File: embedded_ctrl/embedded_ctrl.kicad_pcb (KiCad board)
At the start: 2 copper layers, 67.8 x 54.5 mm, 15 parts, among them J1 Conn_02x13_Odd_Even, J3 Conn_01x15_Socket, J4 Conn_01x15_Socket, J6 Screw_Terminal_01x02

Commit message: more work on embedded ctrlr
same-o
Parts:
- removed J3, J4: Conn_01x15_Socket, Connector_PinSocket_2.54mm:PinSocket_1x15_P2.54mm_Vertical
- added C6: 100nF, Capacitor_SMD:C_0603_1608Metric, F.Cu at (134.1, 86.1)
- added C7: 100nF, Capacitor_SMD:C_0603_1608Metric, F.Cu at (131.1, 87.6)
- added C8: 100nF, Capacitor_SMD:C_0603_1608Metric, F.Cu at (101.6, 80.3)
- added C9: 10uF, Capacitor_SMD:CP_Elec_5x5.8, F.Cu at (136.9, 57.8)
- added D1: D_TVS, Diode_SMD:D_0603_1608Metric, F.Cu at (100.1, 80.3)
- added D2: D_TVS, Diode_SMD:D_0603_1608Metric, F.Cu at (100.1, 74.9)
- added D3: D_TVS, Diode_SMD:D_0603_1608Metric, F.Cu at (100.1, 83.6)
- added D4: LED, Diode_SMD:D_0603_1608Metric, F.Cu at (137.7, 52.0)
- added J7: USB_B, Connector_USB:USB_B_OST_USB-B1HSxx_Horizontal, F.Cu at (96.7, 81.7)
- added Q1: SS8050, Package_TO_SOT_SMD:SOT-23, F.Cu at (104.1, 65.0)
- added Q2: SS8050, Package_TO_SOT_SMD:SOT-23, F.Cu at (109.2, 68.6)
- added R10: 0R, Resistor_SMD:R_0603_1608Metric, F.Cu at (105.7, 72.4)
- added R11: 0R, Resistor_SMD:R_0603_1608Metric, F.Cu at (105.7, 70.9)
- added R12: 10k, Resistor_SMD:R_0603_1608Metric, F.Cu at (103.4, 68.5)
- added R13: 10k, Resistor_SMD:R_0603_1608Metric, F.Cu at (105.7, 67.8)
- added R14: 0R, Resistor_SMD:R_0603_1608Metric, F.Cu at (105.7, 69.3)
- added R15: 2k (5%), Resistor_SMD:R_0603_1608Metric, F.Cu at (135.9, 52.1)
- added R5: 10k, Resistor_SMD:R_0603_1608Metric, F.Cu at (132.6, 86.1)
- added R6: 22.1k (1%), Resistor_SMD:R_0603_1608Metric, F.Cu at (102.9, 82.8)
- added R7: 47.5k (1%), Resistor_SMD:R_0603_1608Metric, F.Cu at (102.9, 84.3)
- added R8: 2k (5%), Resistor_SMD:R_0603_1608Metric, F.Cu at (104.1, 81.0)
- added R9: DNP, Resistor_SMD:R_0603_1608Metric, F.Cu at (106.9, 81.9)
- added REF**: RJ14_Connfly_DS1133-S4_Horizontal, Connector_RJ:RJ14_Connfly_DS1133-S4_Horizontal, F.Cu at (93.7, 39.9)
- added U1: ESP32-WROOM-32, RF_Module:ESP32-WROOM-32, F.Cu at (120.0, 79.9)
- added U2: CP2102N-A02-GQFN28, Package_DFN_QFN:QFN-28-1EP_5x5mm_P0.5mm_EP3.35x3.35mm, F.Cu at (105.2, 76.6)
- added U3: R-78E3.3-1.0, Converter_DCDC:Converter_DCDC_RECOM_R-78E-0.5_THT, F.Cu at (110.7, 59.1)
- moved C5 42.1 mm to (100.6, 54.6), turned to -90 degrees
- moved J6 32.2 mm to (130.8, 55.1)
- moved C2 29.5 mm to (139.4, 84.1), turned to 0 degrees
- moved C3 29.1 mm to (139.4, 86.9), turned to 0 degrees
- moved R2 28.2 mm to (136.4, 84.1), turned to 0 degrees
- moved C4 27.0 mm to (138.1, 88.4), turned to 0 degrees
- moved R3 25.9 mm to (136.4, 86.9), turned to 0 degrees
- moved C1 24.4 mm to (139.4, 82.3), turned to 0 degrees
- moved R4 24.4 mm to (135.1, 88.4), turned to 0 degrees
- moved R1 22.9 mm to (136.4, 82.3), turned to 0 degrees
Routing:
- net 5V: track 0.00 -> 32.2 mm
- net 3V3: track 0.00 -> 30.2 mm, vias 0 -> 1
- net /RXD0_ESP: track 0.00 -> 15.3 mm
- net /TXD0_ESP: track 0.00 -> 14.9 mm
- net /~{RTS}: track 0.00 -> 8.76 mm
- net D34: track 0.00 -> 8.64 mm
- net D35: track 0.00 -> 7.94 mm
- net D19: track 0.00 -> 7.76 mm
- net D32: track 0.00 -> 7.17 mm
- net /~{DTR}: track 0.00 -> 6.48 mm
- net Net-(U2-VBUS): track 0.00 -> 5.61 mm
- net EN: track 0.00 -> 5.49 mm
- net /TXD_BRIDGE: track 0.00 -> 4.35 mm
- net /IO0: track 0.00 -> 3.48 mm
- net Net-(U2-~{SUSPEND}): track 0.00 -> 2.98 mm
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
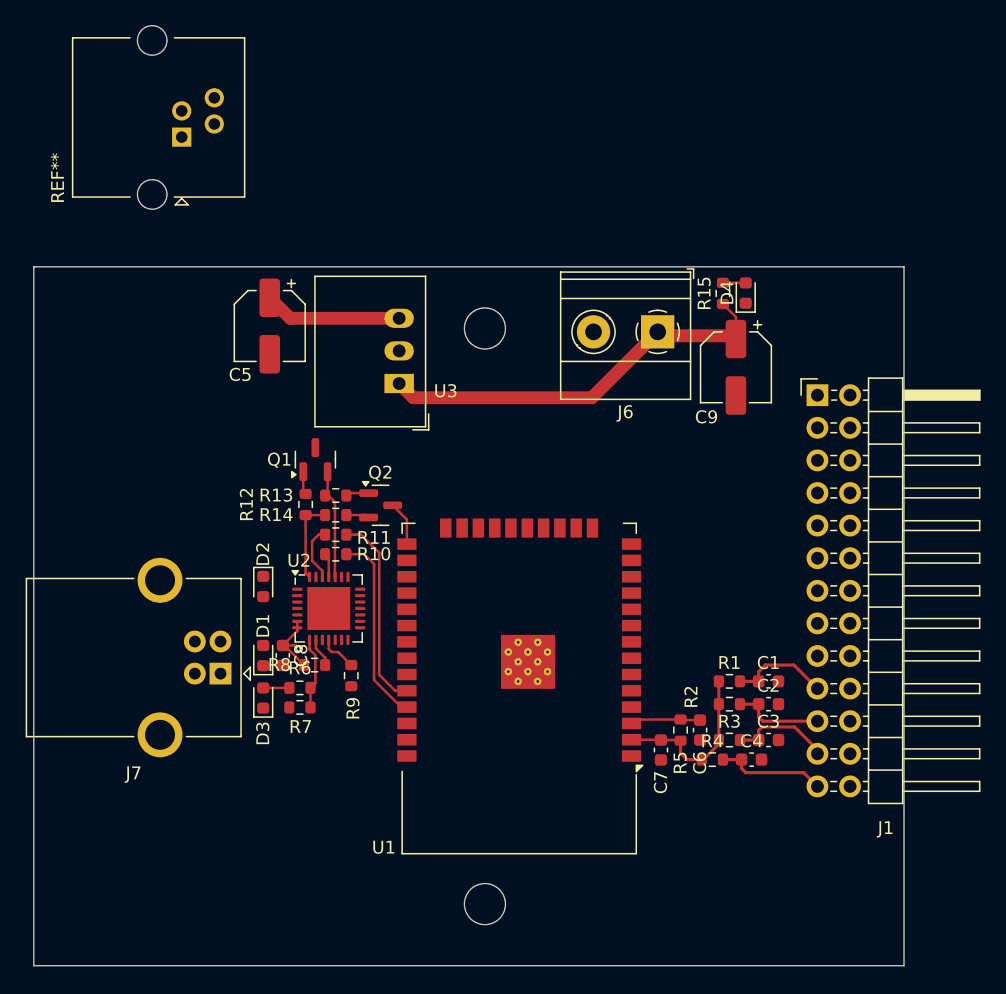
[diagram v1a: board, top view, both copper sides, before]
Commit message: add rj11 connectors for pendants
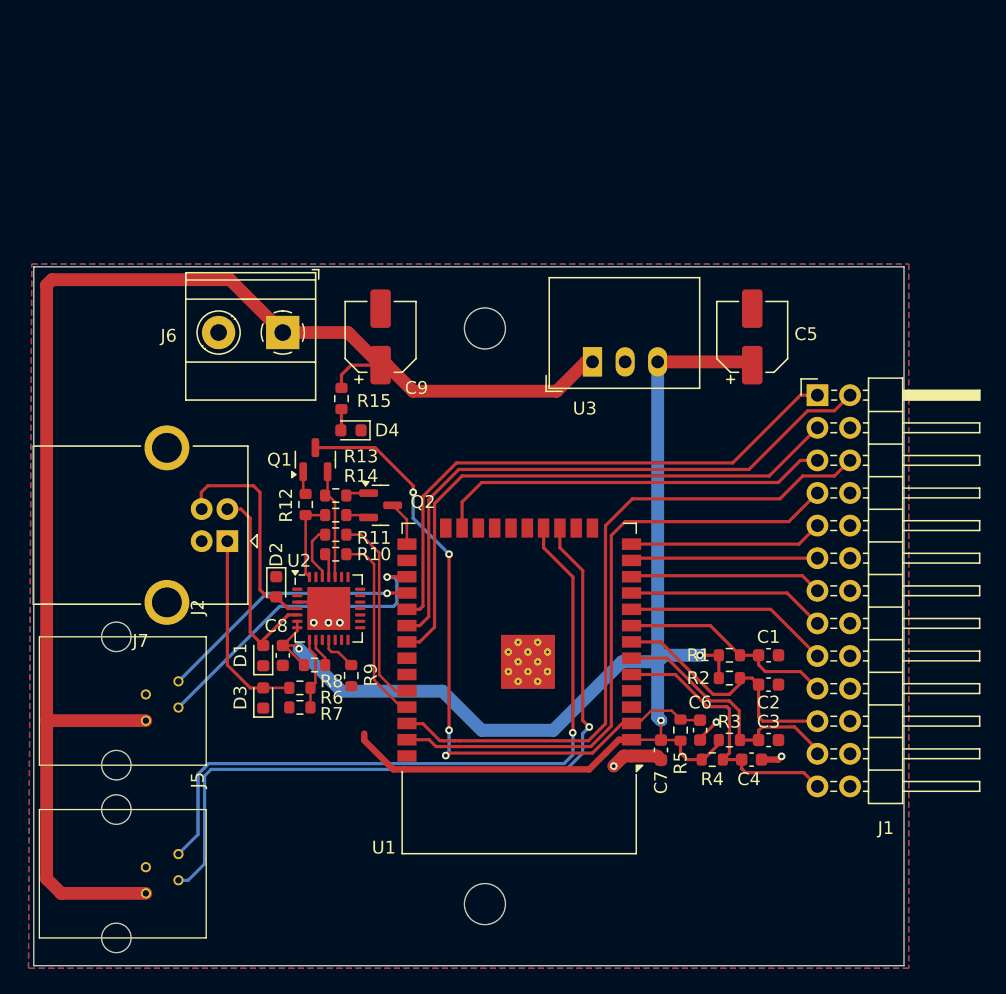
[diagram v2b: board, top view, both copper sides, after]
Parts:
- removed REF**: RJ14_Connfly_DS1133-S4_Horizontal, Connector_RJ:RJ14_Connfly_DS1133-S4_Horizontal
- added J2: RJ11, Library:RJ11_C189737, F.Cu at (93.5, 83.8)
- added J5: RJ11, Library:RJ11_C189737, F.Cu at (93.5, 97.3)
- C5, C9: footprint Capacitor_SMD:CP_Elec_5x5.8 -> Capacitor_SMD:CP_Elec_5x5.4
- moved C5 37.6 mm to (138.2, 55.5), turned to 90 degrees
- moved D4 32.6 mm to (106.9, 62.7), turned to 180 degrees
- moved R15 30.8 mm to (106.2, 60.3), turned to -90 degrees
- moved J6 29.2 mm to (101.6, 55.1)
- moved C9 27.8 mm to (109.2, 55.5), turned to 90 degrees
- moved U3 15.2 mm to (125.7, 57.4), turned to 0 degrees
- moved J7 10.3 mm to (97.3, 71.4)
- moved C1 2.03 mm to (139.4, 80.3)
- moved R1 2.03 mm to (136.4, 80.3)
- moved R2 2.03 mm to (136.4, 82.0)
- moved C2 1.52 mm to (139.4, 82.5)
- moved D2 1.02 mm to (101.1, 74.9)
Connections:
- C1 pad 1: D19 -> D33
- J1 pad 11: D26 -> D14
- J1 pad 15: D33 -> D26
- J1 pad 19: D19 -> D33
- J1 pad 3: D22 -> D19
- J1 pad 6: D23 -> D22
- J1 pad 7: D14 -> D23
- R1 pad 2: D19 -> D33
- U1 pad 10: unconnected-(U1-IO25-Pad10) -> D25
- U1 pad 11: unconnected-(U1-IO26-Pad11) -> D26
- U1 pad 12: unconnected-(U1-IO27-Pad12) -> D27
- U1 pad 13: unconnected-(U1-IO14-Pad13) -> D14
- U1 pad 14: unconnected-(U1-IO12-Pad14) -> D12
- U1 pad 17: unconnected-(U1-SHD/SD2-Pad17) -> /U1RXD
- U1 pad 18: unconnected-(U1-SWP/SD3-Pad18) -> /U1TXD
- U1 pad 23: unconnected-(U1-IO15-Pad23) -> D15
- U1 pad 27: unconnected-(U1-IO16-Pad27) -> /U2RXD
- U1 pad 28: unconnected-(U1-IO17-Pad28) -> /U2TXD
- U1 pad 29: unconnected-(U1-IO5-Pad29) -> D5
- U1 pad 30: unconnected-(U1-IO18-Pad30) -> D18
- U1 pad 31: unconnected-(U1-IO19-Pad31) -> D19
- U1 pad 36: unconnected-(U1-IO22-Pad36) -> D22
- U1 pad 37: unconnected-(U1-IO23-Pad37) -> D23
- U1 pad 6: unconnected-(U1-IO34-Pad6) -> D34
- U1 pad 7: unconnected-(U1-IO35-Pad7) -> D35
- U1 pad 8: unconnected-(U1-IO32-Pad8) -> D32
- U1 pad 9: unconnected-(U1-IO33-Pad9) -> D33
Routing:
- net 3V3: track 30.2 -> 115.2 mm, vias 1 -> 3
- net 5V: track 32.2 -> 113.8 mm
- net /U1RXD: track 0.00 -> 58.3 mm, vias 0 -> 1
- net /U1TXD: track 0.00 -> 55.3 mm, vias 0 -> 1
- net D22: track 0.00 -> 53.2 mm
- net D23: track 0.00 -> 49.1 mm
- net D18: track 0.00 -> 47.3 mm
- net EN: track 5.49 -> 52.7 mm, vias 0 -> 4
- net D5: track 0.00 -> 43.9 mm
- net D19: track 7.76 -> 44.5 mm
- net D15: track 0.00 -> 31.1 mm
- net /U2RXD: track 0.00 -> 24.6 mm, vias 0 -> 1
- net /U2TXD: track 0.00 -> 20.6 mm, vias 0 -> 1
- net /D+: track 0.00 -> 17.4 mm
- net D33: track 0.00 -> 17.0 mm
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- added copper zone on B.Cu, net GND
- added copper zone on F.Cu, net GND

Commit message: improve pcb layout
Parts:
- moved R1 3.31 mm to (139.7, 80.5), turned to 90 degrees
- moved C1 3.16 mm to (136.6, 78.9), turned to -90 degrees
- moved R7 3.10 mm to (105.9, 85.2), turned to 90 degrees
- moved R6 2.77 mm to (104.4, 85.2), turned to 90 degrees
- moved D3 2.75 mm to (100.3, 86.3), turned to -90 degrees
- moved R2 2.70 mm to (139.0, 82.9), turned to 180 degrees
- moved C2 2.44 mm to (138.2, 80.5), turned to 90 degrees
- moved R8 1.44 mm to (105.1, 82.0)
- moved C6 1.27 mm to (134.1, 84.8)
- moved R5 1.27 mm to (132.6, 84.8)
- moved C3 1.27 mm to (139.4, 85.6)
- moved C4 1.27 mm to (138.1, 87.1)
- moved C7 1.27 mm to (131.1, 86.4)
- moved R3 1.27 mm to (136.4, 85.6)
- moved R4 1.27 mm to (135.1, 87.1)
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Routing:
- net 3V3: track 115.2 -> 135.7 mm, vias 3 -> 0
- net /VBUS: track 15.2 -> 24.4 mm, vias 0 -> 2
- net Net-(U2-VBUS): track 5.61 -> 7.71 mm
- net Net-(U2-~{RST}): track 2.26 -> 3.69 mm
- net D32: track 19.8 -> 18.8 mm
- net EN: track 52.7 -> 53.5 mm
- net Net-(U2-~{SUSPEND}): track 2.98 -> 3.51 mm
- net GND: track 10.4 -> 10.7 mm, vias 6 -> 34

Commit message: same
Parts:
- added TP1: VBUS, TestPoint:TestPoint_THTPad_D1.0mm_Drill0.5mm, F.Cu at (99.9, 86.2)
- added TP2: 3V3, TestPoint:TestPoint_THTPad_D1.0mm_Drill0.5mm, F.Cu at (140.7, 94.6)
- added TP3: 5V, TestPoint:TestPoint_THTPad_D1.0mm_Drill0.5mm, F.Cu at (134.4, 64.1)
- added TP4: GND, TestPoint:TestPoint_THTPad_D1.0mm_Drill0.5mm, F.Cu at (111.5, 55.0)
- moved C5 43.1 mm to (144.7, 98.0), turned to -90 degrees
- moved J6 27.3 mm to (128.9, 55.0)
- moved C9 19.3 mm to (126.6, 63.8), turned to 180 degrees
- moved R15 13.9 mm to (120.0, 61.7), turned to 180 degrees
- moved U3 13.3 mm to (138.9, 59.5), turned to 90 degrees
- moved D4 9.58 mm to (116.4, 61.7), turned to 0 degrees
- moved D3 4.22 mm to (97.7, 83.1), turned to 180 degrees
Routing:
- net 5V: track 113.8 -> 145.4 mm
- net 3V3: track 135.7 -> 133.4 mm
- net /VBUS: track 24.4 -> 25.2 mm, vias 2 -> 1
- net GND: vias 34 -> 63

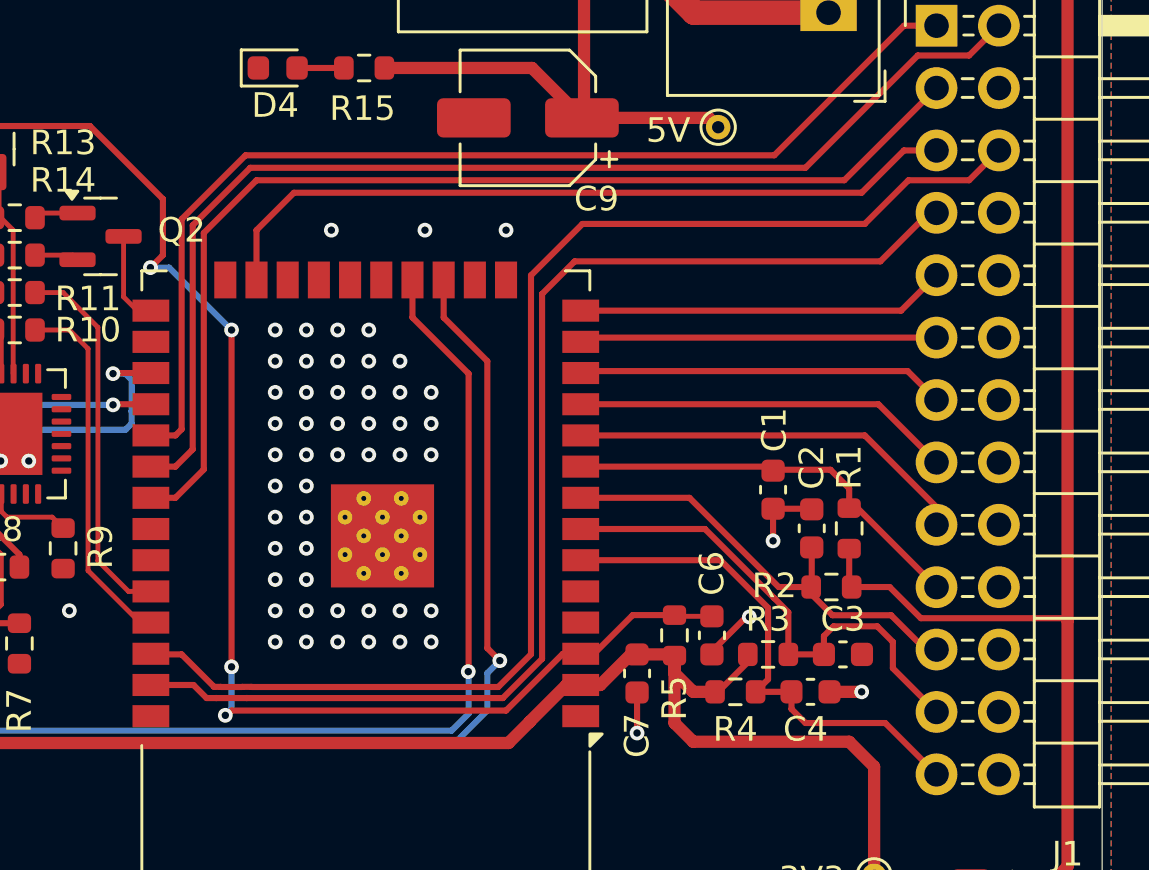
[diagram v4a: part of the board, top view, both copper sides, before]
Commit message: Reassign pins to free up JTAG pins, just in case
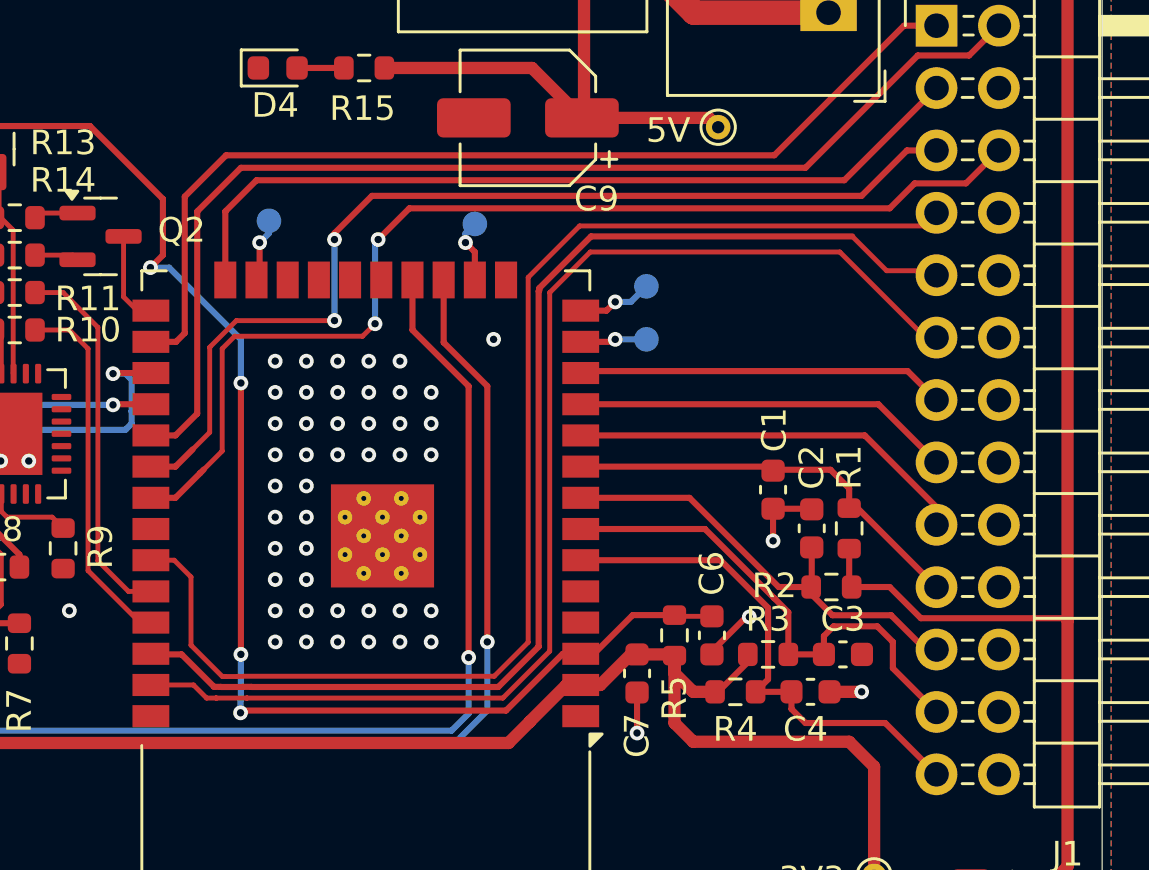
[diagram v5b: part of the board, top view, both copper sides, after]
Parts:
- added TP5: MTDI, TestPoint:TestPoint_Pad_D1.0mm, B.Cu at (131.4, 70.6)
- added TP6: MTCK, TestPoint:TestPoint_Pad_D1.0mm, B.Cu at (124.5, 68.1)
- added TP7: MTMS, TestPoint:TestPoint_Pad_D1.0mm, B.Cu at (131.4, 72.8)
- added TP8: MTDO, TestPoint:TestPoint_Pad_D1.0mm, B.Cu at (116.1, 67.9)
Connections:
- J1 pad 1: D5 -> D4
- J1 pad 11: D14 -> D23
- J1 pad 2: D18 -> D5
- J1 pad 3: D19 -> D2
- J1 pad 5: D15 -> D18
- J1 pad 6: D22 -> D19
- J1 pad 7: D23 -> D21
- J1 pad 9: D12 -> D22
- U1 pad 13: D14 -> /MTMS
- U1 pad 14: D12 -> /MTDI
- U1 pad 16: unconnected-(U1-IO13-Pad16) -> /MTCK
- U1 pad 23: D15 -> /MTDO
- U1 pad 24: unconnected-(U1-IO2-Pad24) -> D2
- U1 pad 26: unconnected-(U1-IO4-Pad26) -> D4
- U1 pad 33: unconnected-(U1-IO21-Pad33) -> D21
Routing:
- net D21: track 0.00 -> 52.1 mm
- net D4: track 0.00 -> 40.6 mm
- net D2: track 0.00 -> 33.8 mm
- net D15: track 31.1 -> 0.00 mm
- net D12: track 15.1 -> 0.00 mm
- net D14: track 14.6 -> 0.00 mm
- net D18: track 47.3 -> 41.4 mm, vias 0 -> 2
- net D22: track 53.2 -> 49.3 mm
- net /MTDI: track 0.00 -> 3.09 mm, vias 0 -> 1
- net /MTMS: track 0.00 -> 2.72 mm, vias 0 -> 1
- net /MTDO: track 0.00 -> 2.62 mm, vias 0 -> 1
- net /MTCK: track 0.00 -> 2.60 mm, vias 0 -> 1
- net D5: track 43.9 -> 46.3 mm
- net EN: track 53.5 -> 52.8 mm
- net D23: track 49.1 -> 49.7 mm
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
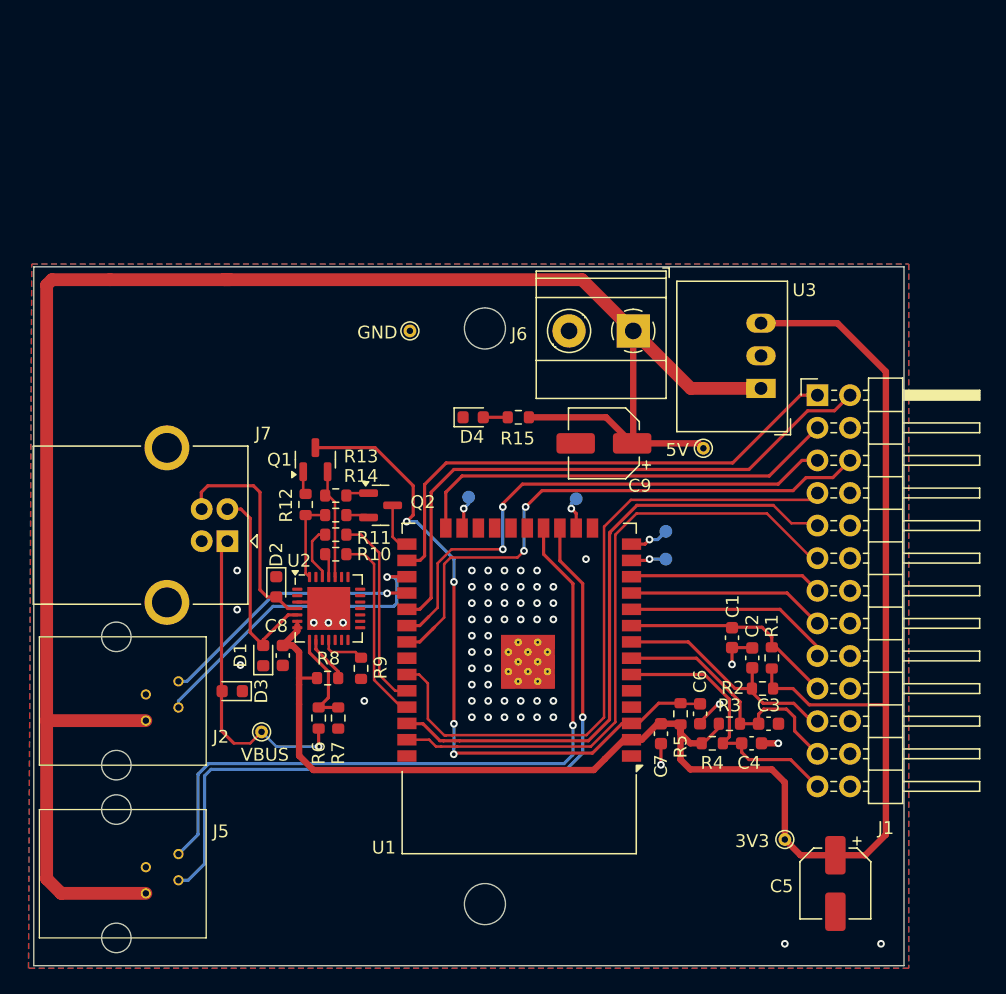
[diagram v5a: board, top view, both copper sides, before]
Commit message: Don't use UART1 - its pins are already in use for the SPI flash
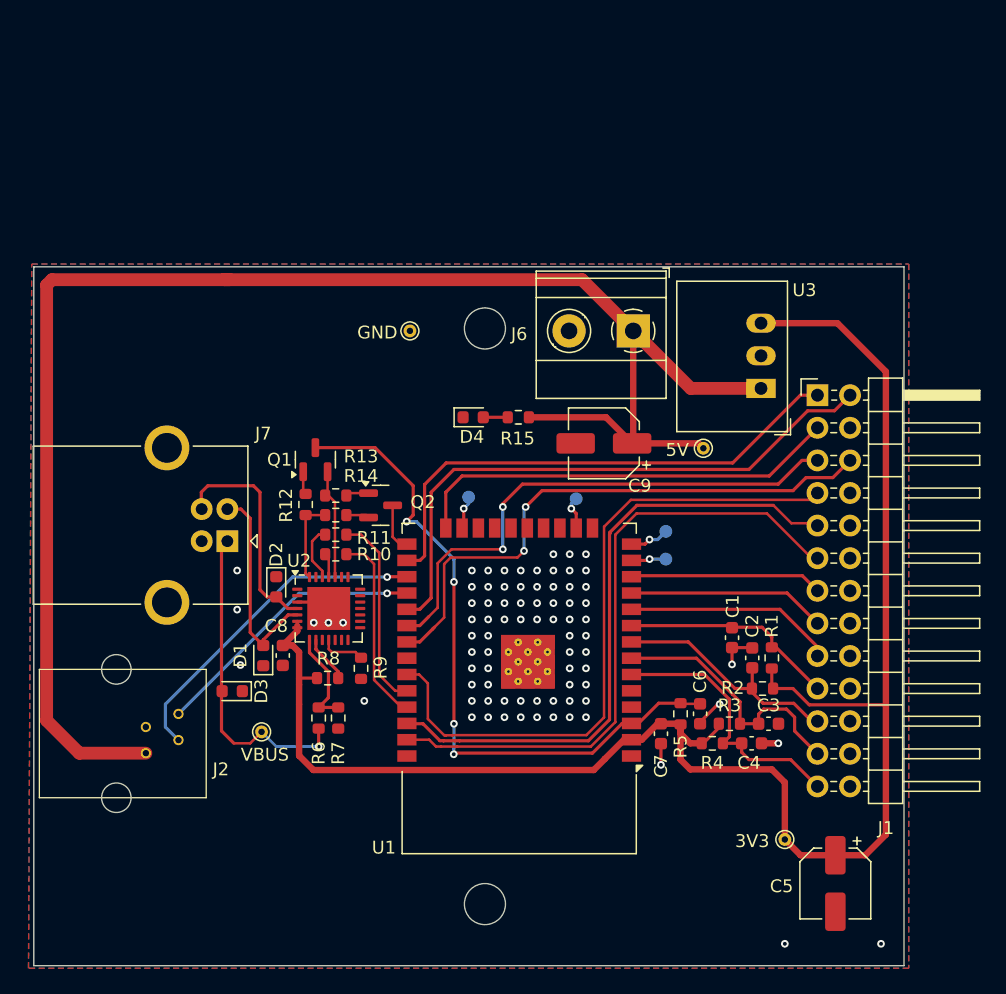
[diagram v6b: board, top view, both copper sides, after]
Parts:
- removed J5: RJ11, Library:RJ11_C189737
- moved J2 2.54 mm to (93.5, 86.4)
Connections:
- U1 pad 17: /U1RXD -> unconnected-(U1-SHD/SD2-Pad17)
- U1 pad 18: /U1TXD -> unconnected-(U1-SWP/SD3-Pad18)
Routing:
- net /U1RXD: track 57.9 -> 0.00 mm, vias 1 -> 0
- net /U1TXD: track 55.3 -> 0.00 mm, vias 1 -> 0
- net 5V: track 145.4 -> 125.9 mm
- net /U2RXD: track 24.9 -> 26.1 mm
- net /U2TXD: track 20.6 -> 21.7 mm
- net GND: vias 57 -> 80
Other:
- board text added: "unusable pins"
